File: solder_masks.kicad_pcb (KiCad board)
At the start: 2 copper layers, 5 parts, among them U1 CAM-M8C, U1 RV-3032, U4 G-NiceRF-GPS, U6 NEO-M8P, U7 SX1276

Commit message: A5 layout
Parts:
- moved U6 64.8 mm to (26.9, 73.2)
- moved U1 64.8 mm to (91.7, 73.3)
- moved U1 64.8 mm to (56.4, 37.2)
- moved U7 64.8 mm to (15.8, 22.1)
- moved U4 64.8 mm to (51.6, 66.4)
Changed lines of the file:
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@@
 		(legacy_teardrops no)
 	)
-	(paper "A4")
+	(paper "A5")
 	(layers
 		(0 "F.Cu" signal)
@@
 	(footprint "MyFootprints:CAM-M8C"
 		(layer "F.Cu")
-		(at 148.082 105.2322)
+		(at 91.7084 73.3044)
 		(tags "CAM-M8C-0 ")
 		(property "Reference" "U1"
@@
 			(polygon
 				(pts
-					(xy 144.316881 98.0447) (xy 151.516881 98.0447) (xy 151.516881 101.9447) (xy 144.316881 101.9447)
+					(xy 87.943281 66.1169) (xy 95.143281 66.1169) (xy 95.143281 70.0169) (xy 87.943281 70.0169)
 				)
 			)
@@
 	(footprint "MyFootprints:RV-3032"
 		(layer "F.Cu")
-		(at 112.7602 69.1604 -90)
+		(at 56.3866 37.2326 -90)
 		(property "Reference" "U1"
 			(at 2.4384 -0.1016 0)
@@
 	(footprint "MyFootprints:G-NiceRF-GPS"
 		(layer "F.Cu")
-		(at 107.939 98.2862)
+		(at 51.5654 66.3584)
 		(property "Reference" "U4"
 			(at 7.5 -2.25 0)
@@
 	(footprint "RF_GPS:ublox_NEO"
 		(layer "F.Cu")
-		(at 83.302541 105.08705 180)
+		(at 26.928941 73.15925 180)
 		(descr "ublox NEO 6/7/8, (https://www.u-blox.com/sites/default/files/NEO-8Q-NEO-M8-FW3_HardwareIntegrationManual_%28UBX-15029985%29_0.pdf)")
 		(tags "GPS ublox NEO 6/7/8")
@@
 	(footprint "MyFootprints:SX1276"
 		(layer "F.Cu")
-		(at 72.1454 54.0634)
+		(at 15.7718 22.1356)
 		(property "Reference" "U7"
 			(at 12.4 21.6 0)
@@
 	)
 	(gr_text "NEO-M8P"
-		(at 76.088941 90.50745 0)
+		(at 19.715341 58.57965 0)
 		(layer "F.Mask")
 		(effects
@@
 	)
 	(gr_text "CAM-M8"
-		(at 141.26574 91.43865 0)
+		(at 84.89214 59.51085 0)
 		(layer "F.Mask")
 		(effects
@@
 	)
 	(gr_text "G-NiceRF"
-		(at 108.2548 90.6526 0)
+		(at 51.8812 58.7248 0)
 		(layer "F.Mask")
 		(effects
@@
 	)
 	(gr_text "LoRa"
-		(at 78.8416 52.5018 0)
+		(at 22.468 20.574 0)
 		(layer "F.Mask")
 		(effects
@@
 	)
 	(gr_text "RV-3032"
-		(at 107.6548 60.88 0)
+		(at 51.2812 28.9522 0)
 		(layer "F.Mask")
 		(effects

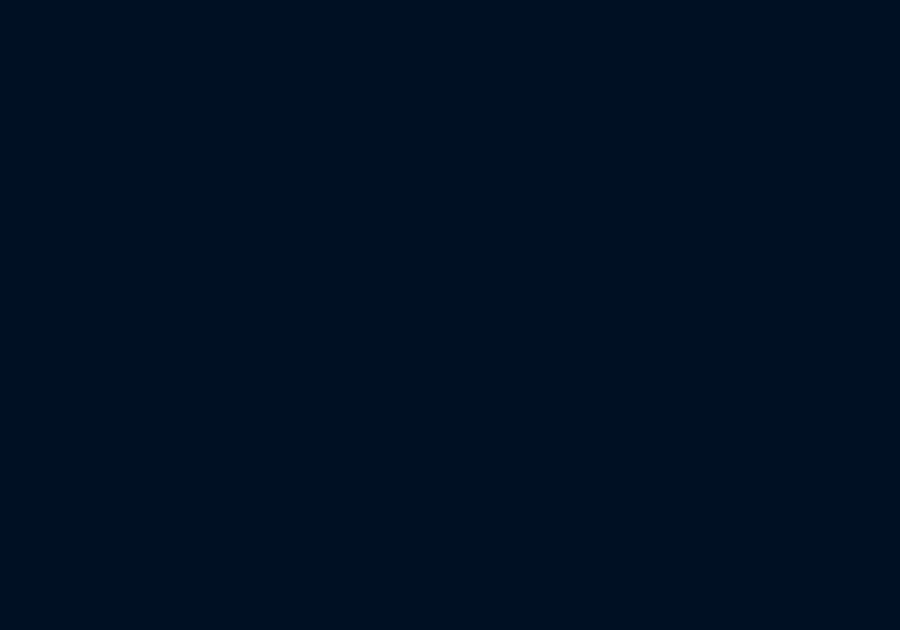
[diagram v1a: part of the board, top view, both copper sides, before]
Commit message: SH1.0 4P connector
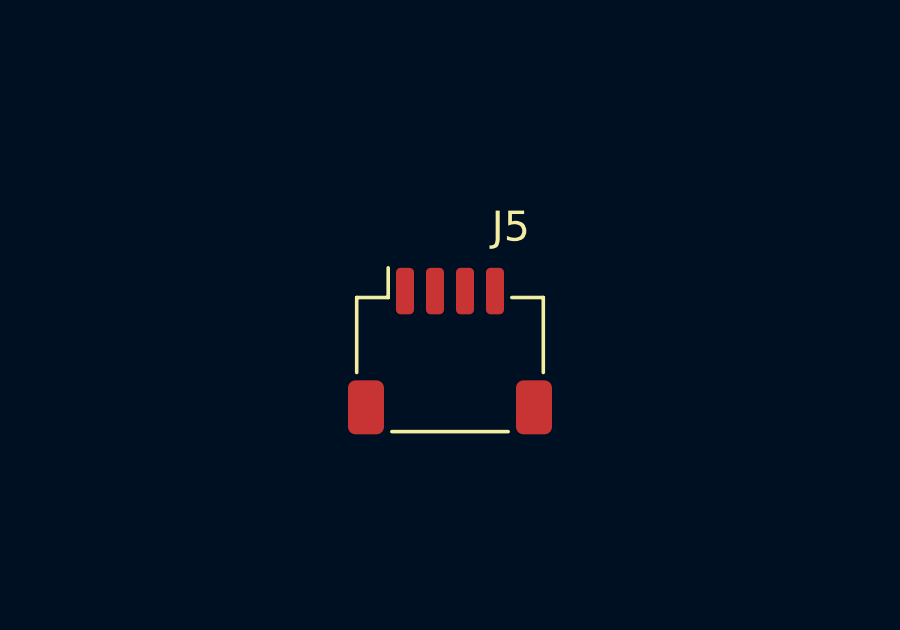
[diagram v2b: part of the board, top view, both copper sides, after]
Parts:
- added J5: SH_Conn_01x04, Connector_JST:JST_SH_SM04B-SRSS-TB_1x04-1MP_P1.00mm_Horizontal, F.Cu at (83.8, 37.3)
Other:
- rule pad_to_mask_clearance: 0.1 -> -0.1

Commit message: sh1.0 vertical
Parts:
- added REF**: JST_SH_BM04B-SRSS-TB_1x04-1MP_P1.00mm_Vertical, Connector_JST:JST_SH_BM04B-SRSS-TB_1x04-1MP_P1.00mm_Vertical, F.Cu at (93.5, 50.8)
